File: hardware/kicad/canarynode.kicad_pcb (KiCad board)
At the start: 4 copper layers, 61 parts, among them J1 Conn_01x02, J2 USB_C_Receptacle_USB2.0_16P, J3 Screw_Terminal_01x03, J4 Conn_01x02, J5 Conn_02x05_Odd_Even, J6 Conn_01x04, SW1 SW_Push, SW2 SW_Push, U1 TPS62160DGK, U2 STM32G474RETx, U3 USBLC6-2P6, U4 BMI270, U5 BME280, U6 TCAN334G

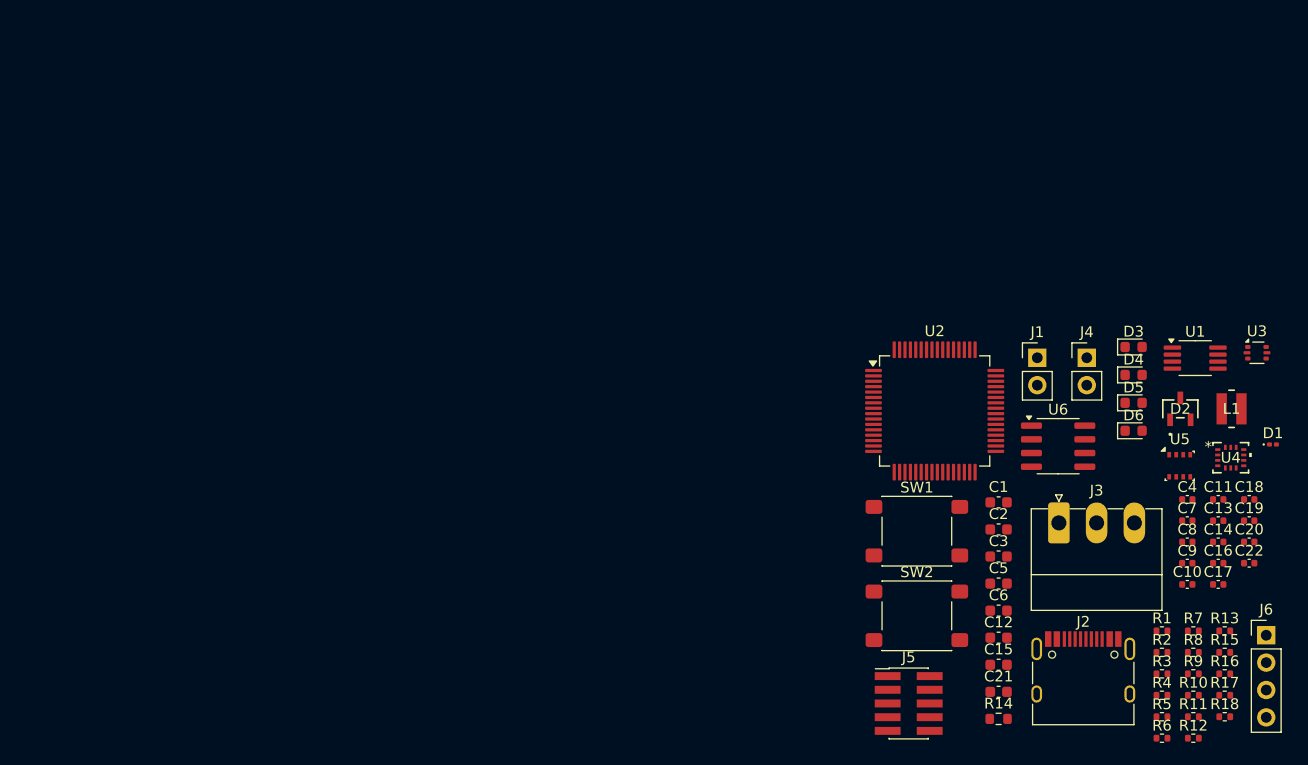
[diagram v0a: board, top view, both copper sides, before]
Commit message: pcb: place edge connectors, MCU, ICs, buck/CAN/MCU decoupling clusters
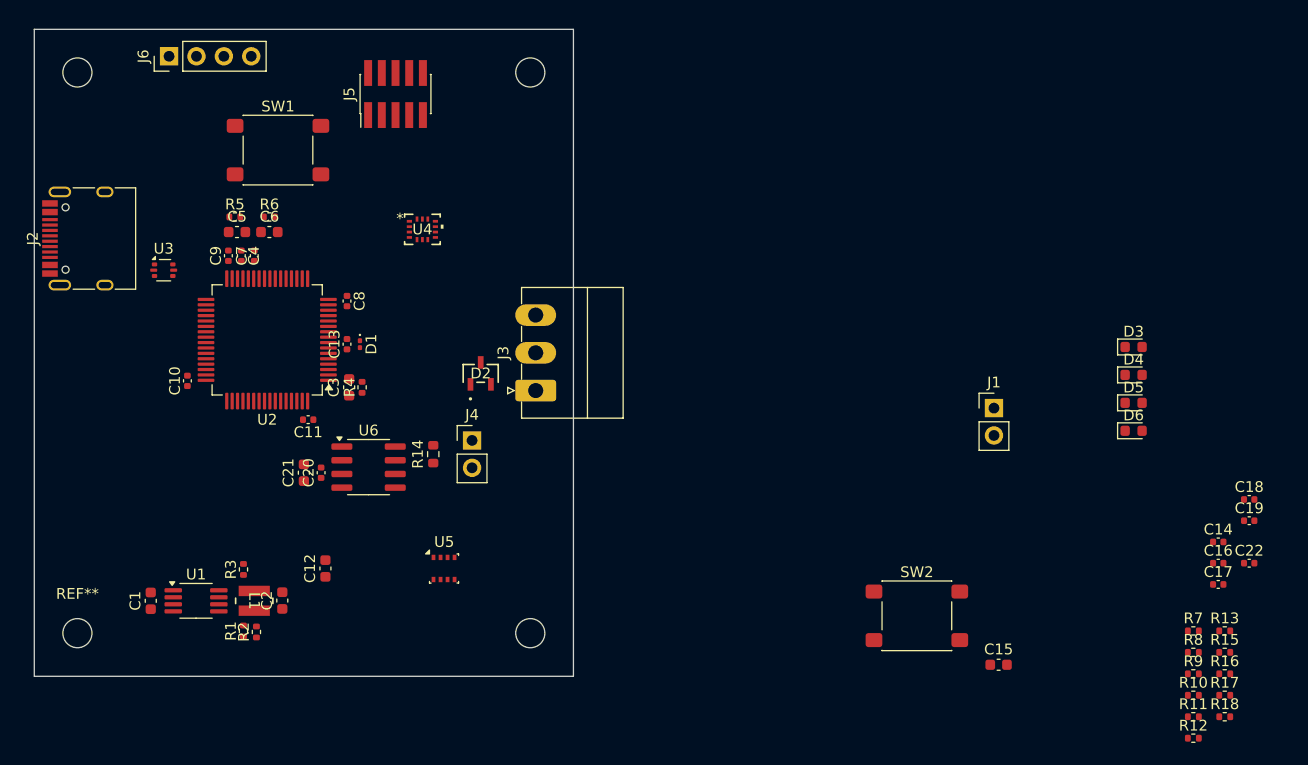
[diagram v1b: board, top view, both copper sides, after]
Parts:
- added ?: , , F.Cu at (96.0, 54.0)
- added ?: , , F.Cu at (96.0, 106.0)
- added ?: , , F.Cu at (54.0, 54.0)
- added REF**: MountingHole_2.7mm_M2.5, MountingHole:MountingHole_2.7mm_M2.5, F.Cu at (54.0, 106.0)
- moved J6 115.0 mm to (62.5, 52.5), turned to 90 degrees
- moved U3 101.7 mm to (62.0, 72.3)
- moved J2 100.6 mm to (55.5, 69.4), turned to 90 degrees
- moved R5 97.7 mm to (68.6, 67.4)
- moved R6 95.9 mm to (71.8, 67.4)
- moved U1 95.4 mm to (65.0, 103.0)
- moved C10 94.6 mm to (64.2, 82.6), turned to 90 degrees
- moved C9 93.4 mm to (68.0, 71.0), turned to 90 degrees
- moved L1 92.4 mm to (70.4, 103.0), turned to -90 degrees
- moved C4 90.6 mm to (69.2, 71.0), turned to -90 degrees
- moved C7 90.0 mm to (70.4, 71.0), turned to 90 degrees
- moved C20 86.3 mm to (76.6, 91.1), turned to 90 degrees
- moved R3 85.7 mm to (69.4, 100.1), turned to 90 degrees
- moved D1 85.2 mm to (80.2, 79.2), turned to -90 degrees
- moved R1 85.2 mm to (69.4, 105.8), turned to 90 degrees
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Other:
- board outline added: 50 x 60 mm

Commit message: pcb: complete component placement — all 61 placed, DRC clean (unrouted)
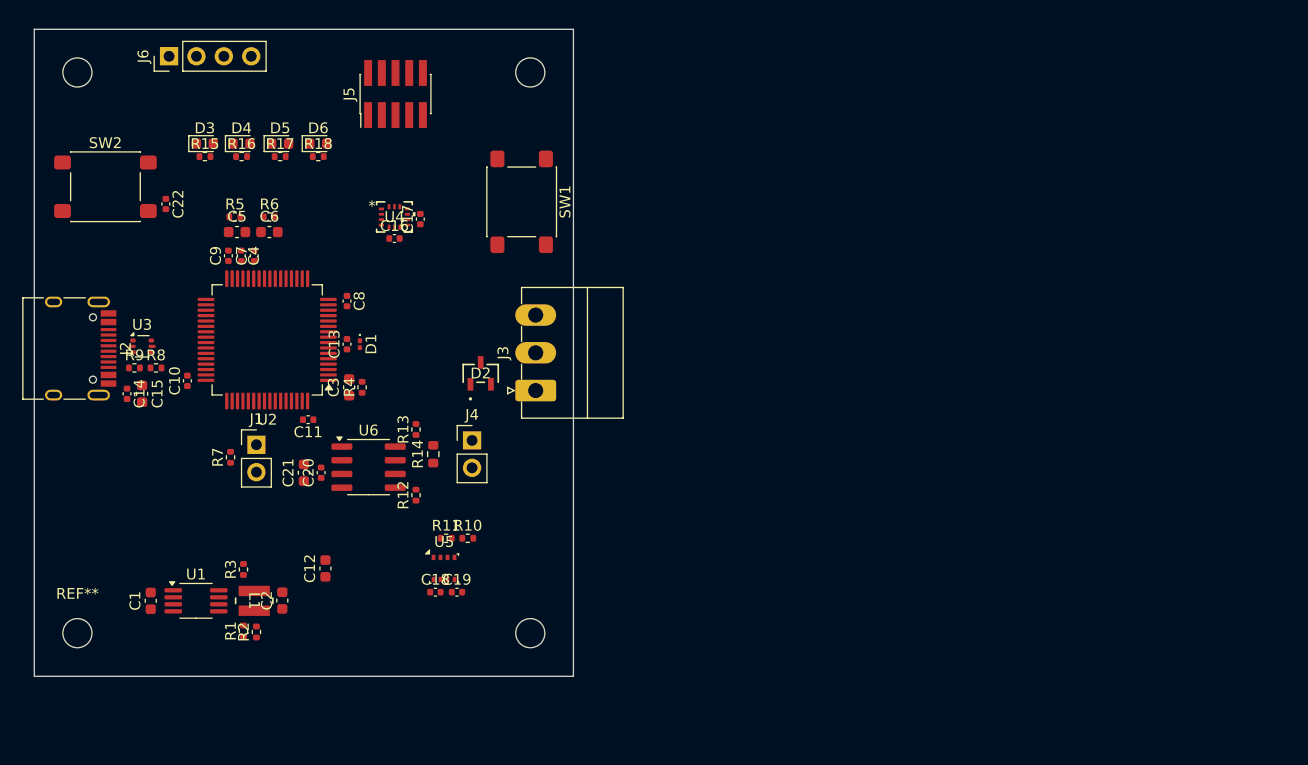
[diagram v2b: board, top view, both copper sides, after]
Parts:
- moved C22 105.8 mm to (62.2, 66.2), turned to -90 degrees
- moved R15 105.2 mm to (65.8, 61.8)
- moved R16 103.0 mm to (69.2, 61.8)
- moved R9 102.2 mm to (59.3, 81.4)
- moved C14 102.1 mm to (58.6, 83.8), turned to -90 degrees
- moved R17 100.8 mm to (72.8, 61.8)
- moved R8 99.8 mm to (61.3, 81.4)
- moved R18 98.8 mm to (76.3, 61.8)
- moved R7 90.7 mm to (68.2, 89.7), turned to 90 degrees
- moved D3 88.2 mm to (65.8, 60.6)
- moved D4 85.5 mm to (69.2, 60.6)
- moved SW2 85.1 mm to (56.6, 64.6)
- moved C15 83.3 mm to (60.0, 83.8), turned to -90 degrees
- moved D5 82.7 mm to (72.8, 60.6)
- moved C16 82.1 mm to (83.4, 69.4)
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
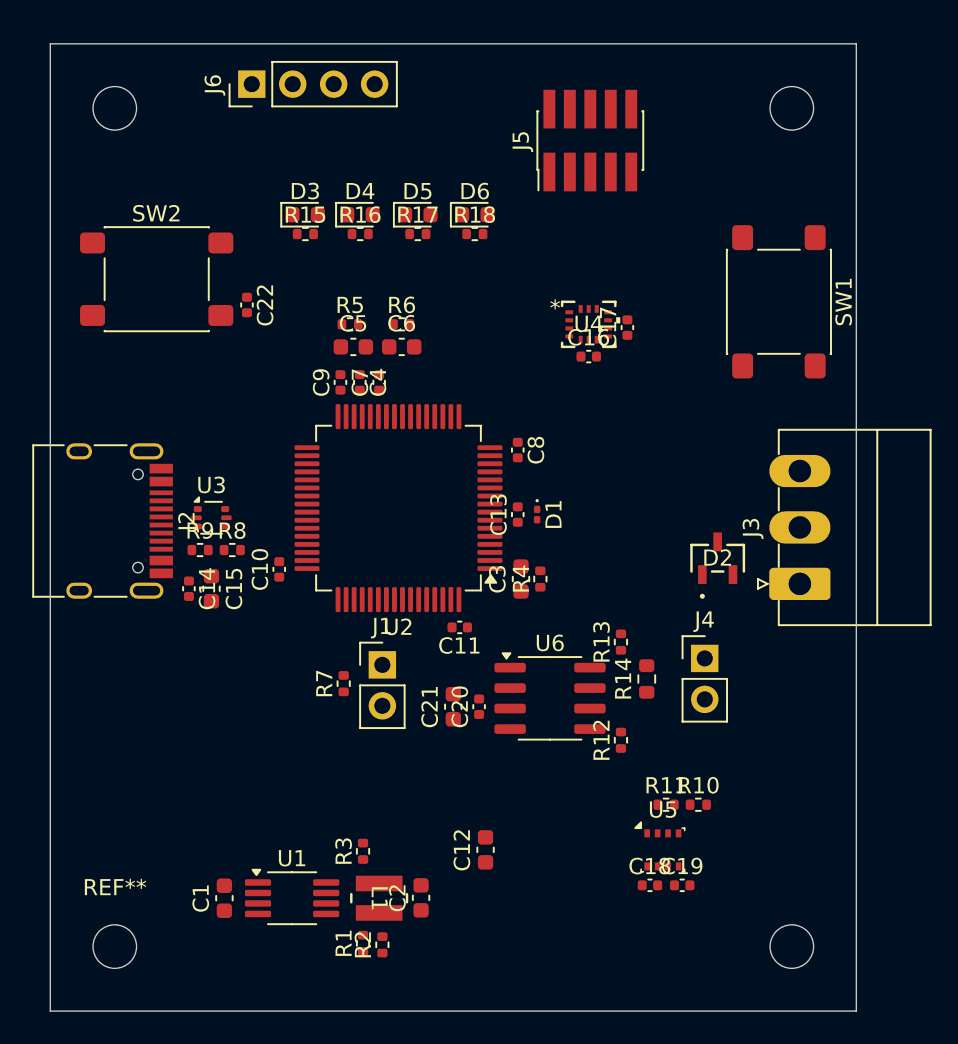
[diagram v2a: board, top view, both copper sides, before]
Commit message: pcb: stitch GND island vias, silkscreen cleanup, DRC clean
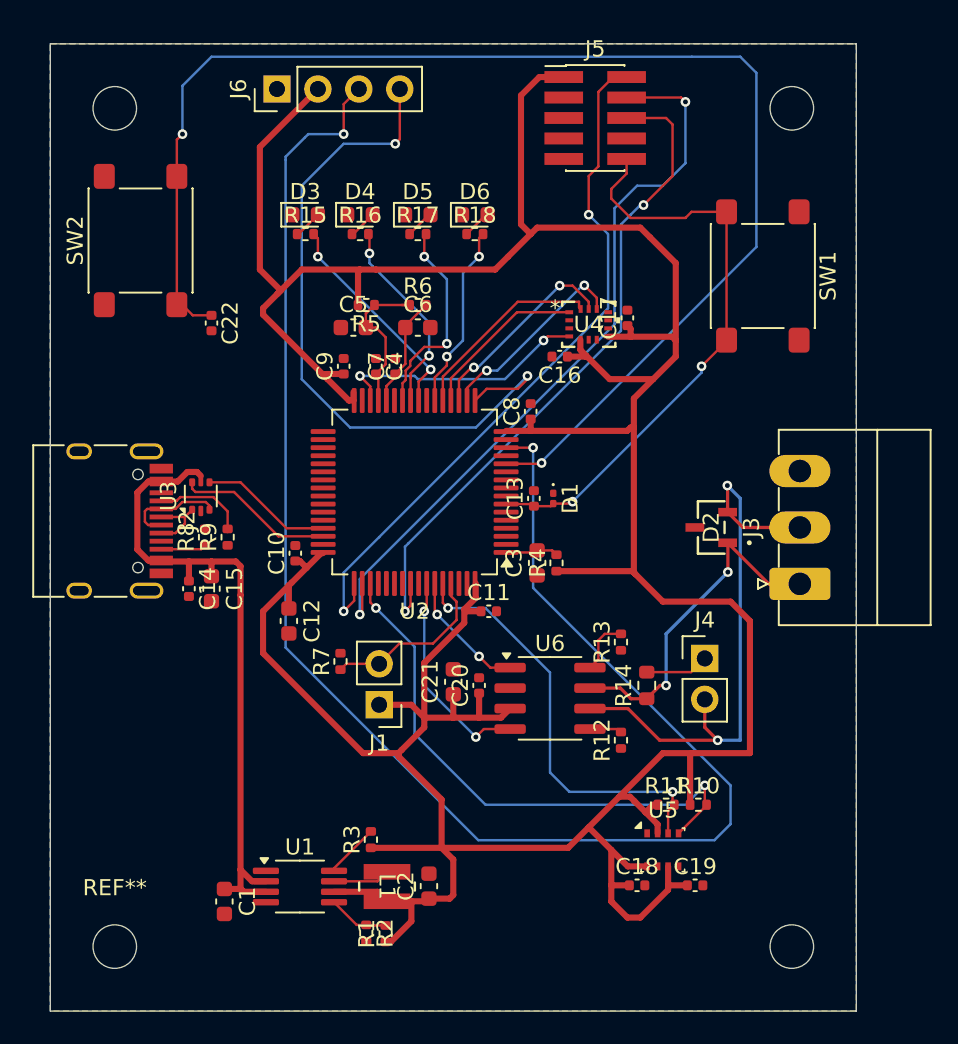
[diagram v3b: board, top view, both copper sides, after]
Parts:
- moved C12 18.7 mm to (64.8, 85.8), turned to -90 degrees
- moved SW2 2.60 mm to (55.6, 62.2), turned to 90 degrees
- moved C8 2.53 mm to (79.8, 72.8), turned to 90 degrees
- moved J1 2.48 mm to (70.4, 91.0), turned to 180 degrees
- moved C22 2.47 mm to (60.0, 67.3)
- moved C11 2.06 mm to (77.2, 85.2), turned to 0 degrees
- moved D2 1.95 mm to (91.0, 80.0), turned to 90 degrees
- moved R9 1.89 mm to (61.0, 80.6), turned to 90 degrees
- moved SW1 1.89 mm to (94.2, 64.4)
- moved R8 1.87 mm to (59.6, 80.6), turned to 90 degrees
- moved C16 1.80 mm to (81.6, 69.4), turned to 180 degrees
- moved J6 1.59 mm to (64.1, 52.8)
- moved C6 1.56 mm to (72.8, 67.6)
- moved R5 1.56 mm to (69.6, 66.2), turned to 180 degrees
- moved R6 1.56 mm to (72.8, 66.2)
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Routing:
- net +3.3V: track 0.00 -> 248.2 mm
- net /USART2_TX: track 0.00 -> 101.0 mm, vias 0 -> 2
- net /BTN1: track 0.00 -> 85.1 mm, vias 0 -> 2
- net /SWCLK: track 0.00 -> 47.1 mm, vias 0 -> 2
- net /SWDIO: track 0.00 -> 44.1 mm, vias 0 -> 2
- net /USART2_RX: track 0.00 -> 43.0 mm, vias 0 -> 2
- net /SWO: track 0.00 -> 42.1 mm, vias 0 -> 2
- net +5V: track 0.00 -> 41.6 mm
- net /NRST: track 0.00 -> 37.1 mm, vias 0 -> 2
- net /CANL: track 0.00 -> 35.7 mm, vias 0 -> 2
- net /I2C1_SCL: track 0.00 -> 34.8 mm, vias 0 -> 2
- net /I2C1_SDA: track 0.00 -> 26.7 mm, vias 0 -> 2
- net /CANH: track 0.00 -> 21.4 mm, vias 0 -> 2
- net /IMU_INT1: track 0.00 -> 16.0 mm, vias 0 -> 2
- net /LED1: track 0.00 -> 13.8 mm, vias 0 -> 2
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- added copper zone on B.Cu, net GND
- added copper zone on F.Cu, net GND
- added copper zone on In1.Cu, net GND
- added copper zone on In2.Cu, net GND

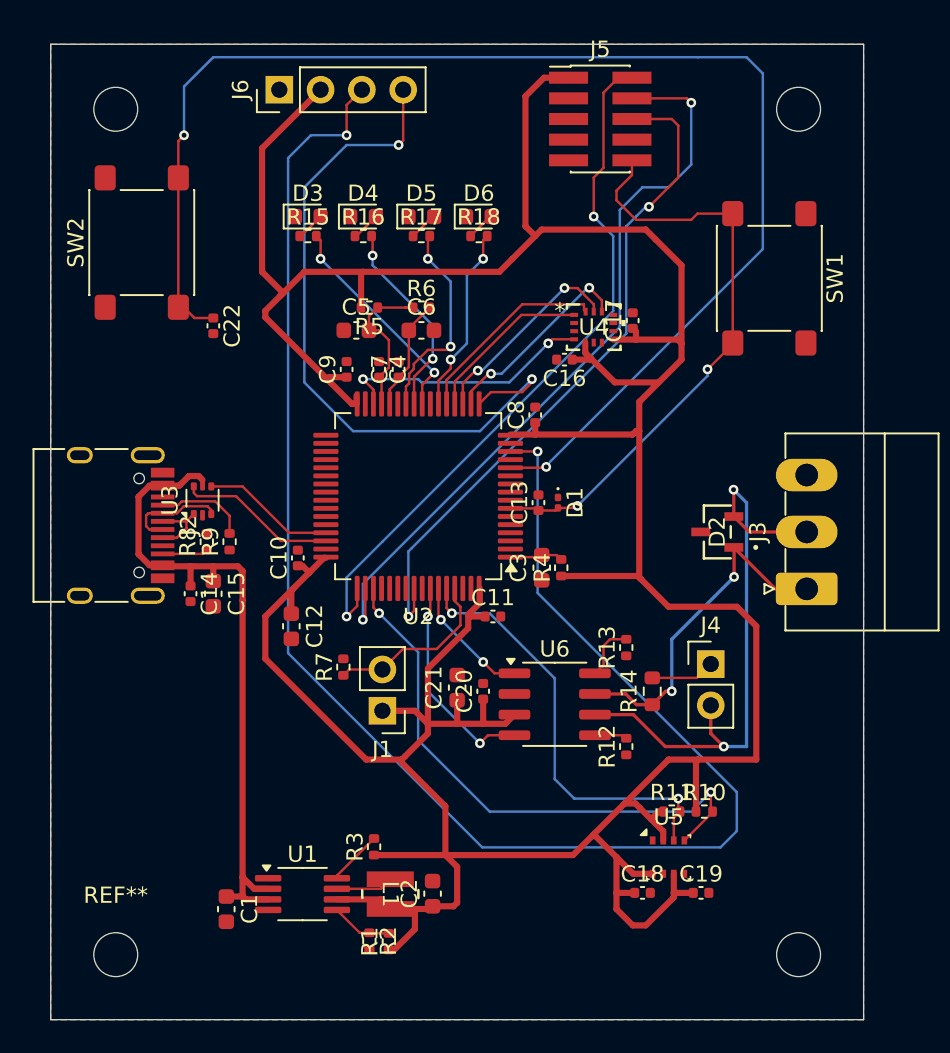
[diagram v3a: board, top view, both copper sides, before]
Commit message: fab: add LCSC to BOM, generate CPL, exclude mounting holes from placement, remove stale datasheet
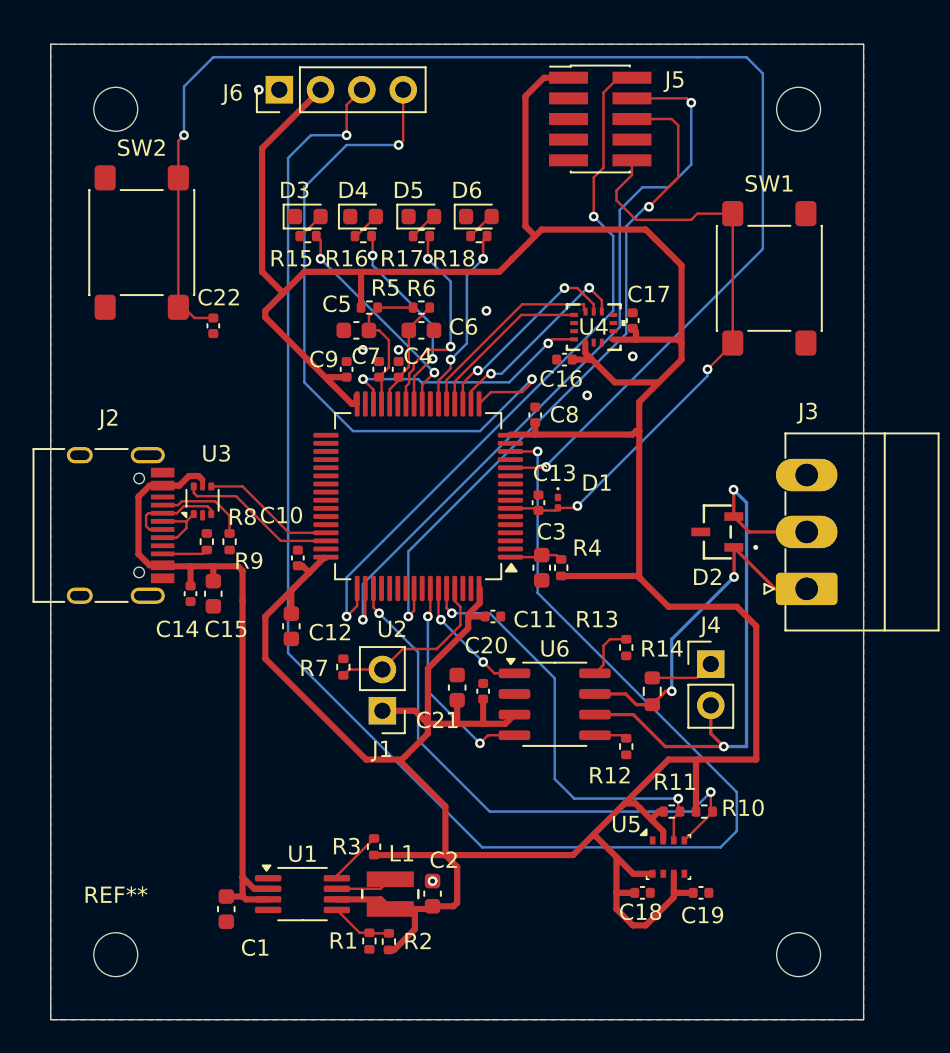
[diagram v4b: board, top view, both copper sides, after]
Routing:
- net GND: vias 0 -> 7
